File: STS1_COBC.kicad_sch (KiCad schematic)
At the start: 13 parts

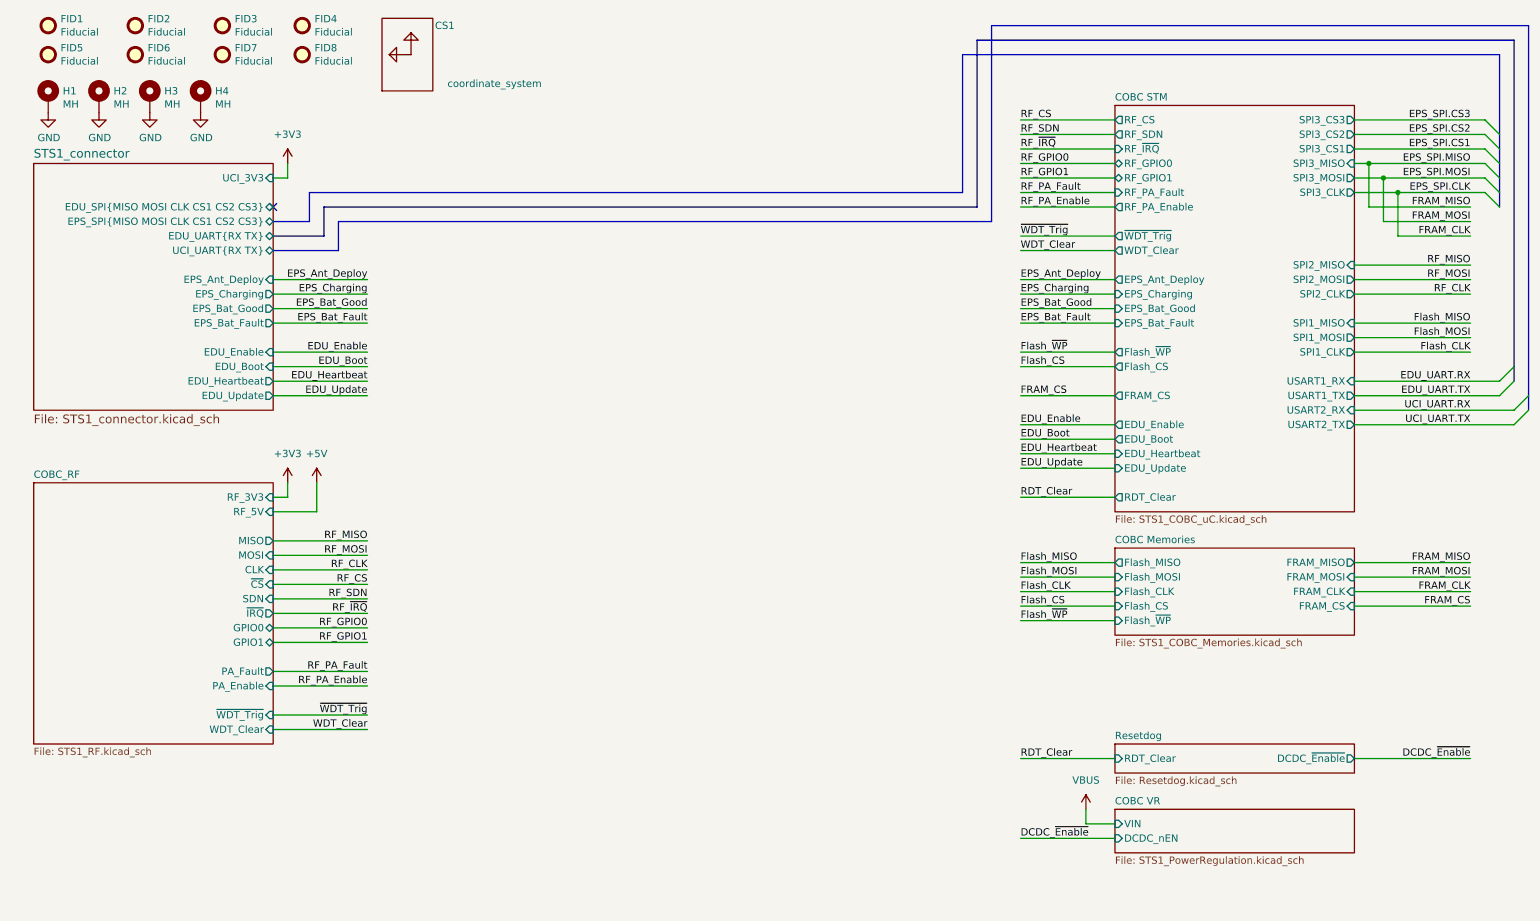
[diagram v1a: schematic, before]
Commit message: Reorganize and clean-up the components around the STM. Pinout changes: 1) Flash_CS moved from PB9 to PA4 2) Dosi_En added on PB10 3) EDU_Boot_Pin added on PB2 4) WDT_Clear moved from PA9 to PB9
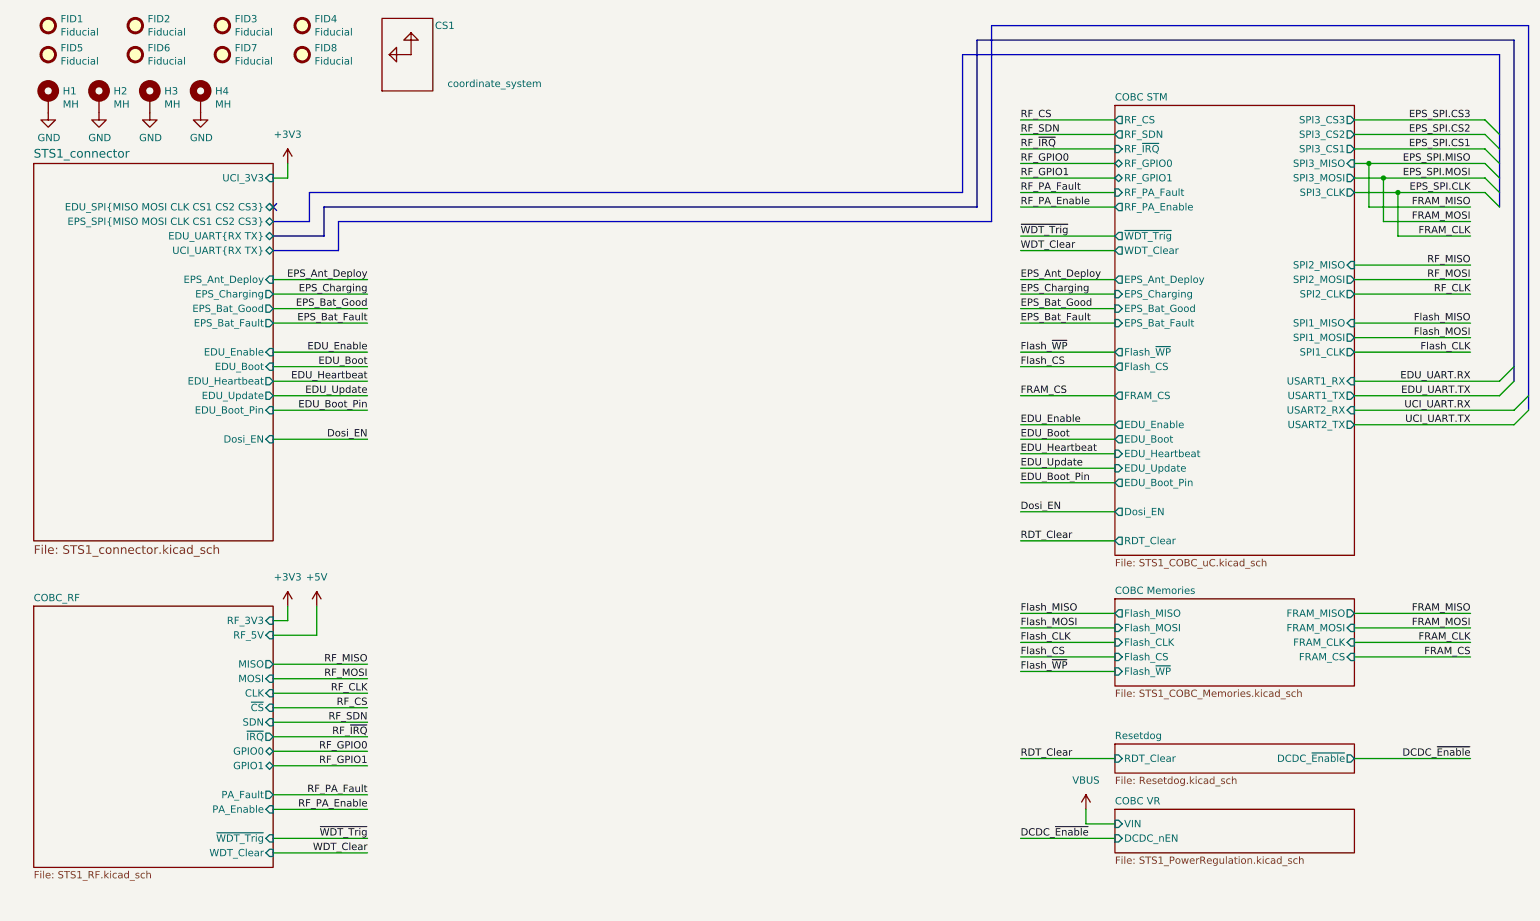
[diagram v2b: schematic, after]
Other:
- sheet COBC STM ports: added Dosi_EN, EDU_Boot_Pin; removed none
- sheet STS1_connector ports: added Dosi_EN, EDU_Boot_Pin; removed none

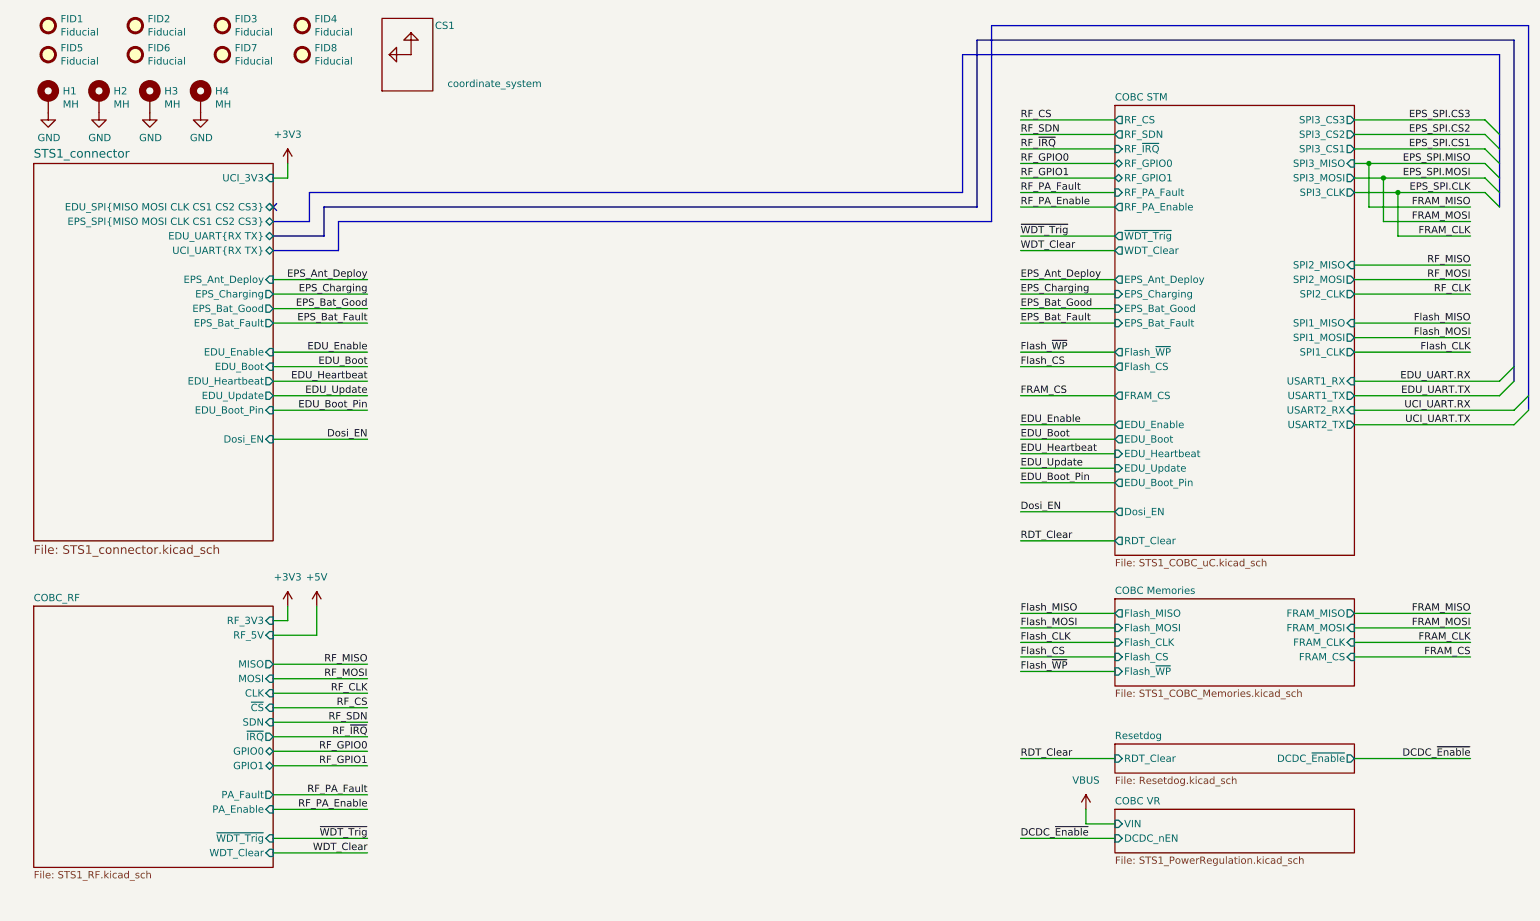
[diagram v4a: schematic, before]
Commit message: Add latchup protection circuits
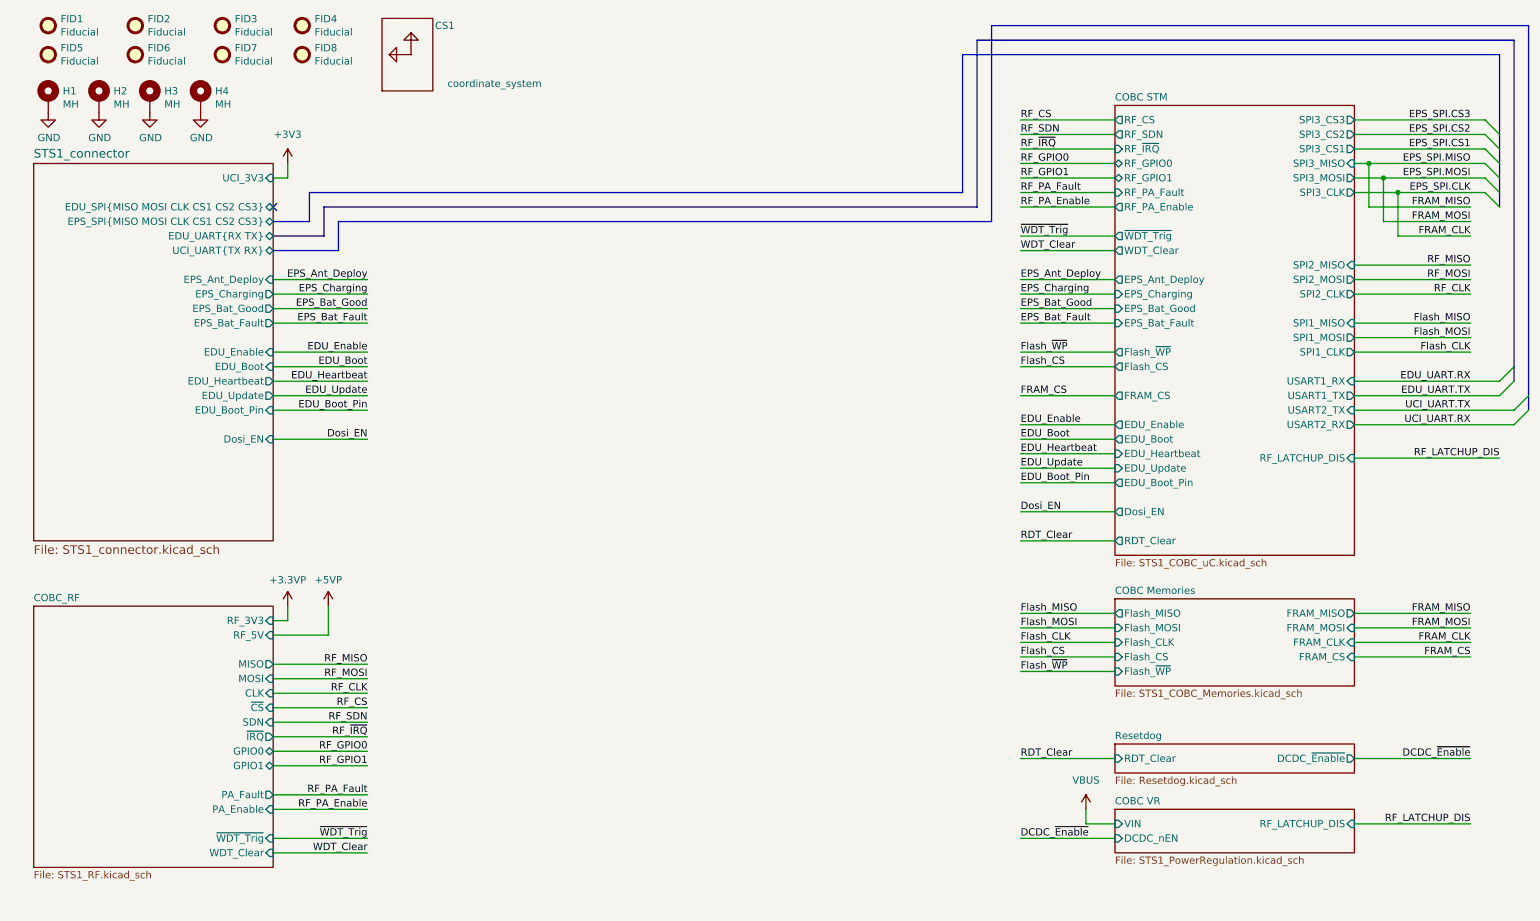
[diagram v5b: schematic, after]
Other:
- sheet COBC STM ports: added RF_LATCHUP_DIS; removed none
- sheet COBC VR ports: added RF_LATCHUP_DIS; removed none
- sheet STS1_connector ports: added UCI_UART{TX RX}; removed UCI_UART{RX TX}

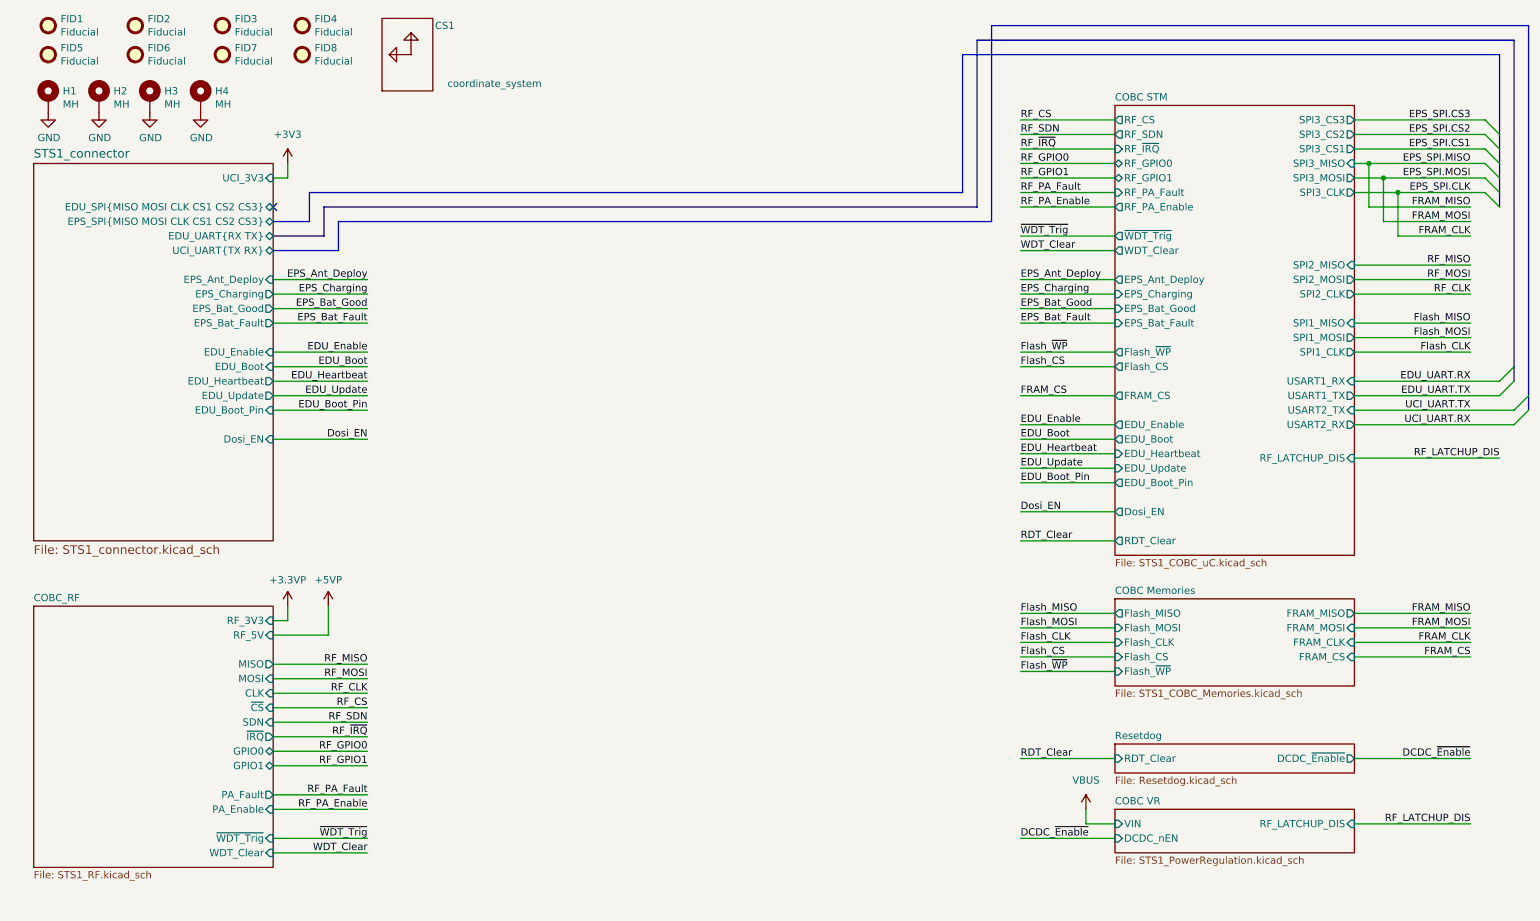
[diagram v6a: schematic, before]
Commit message: Add a temperature sensor near RF amplifier chip
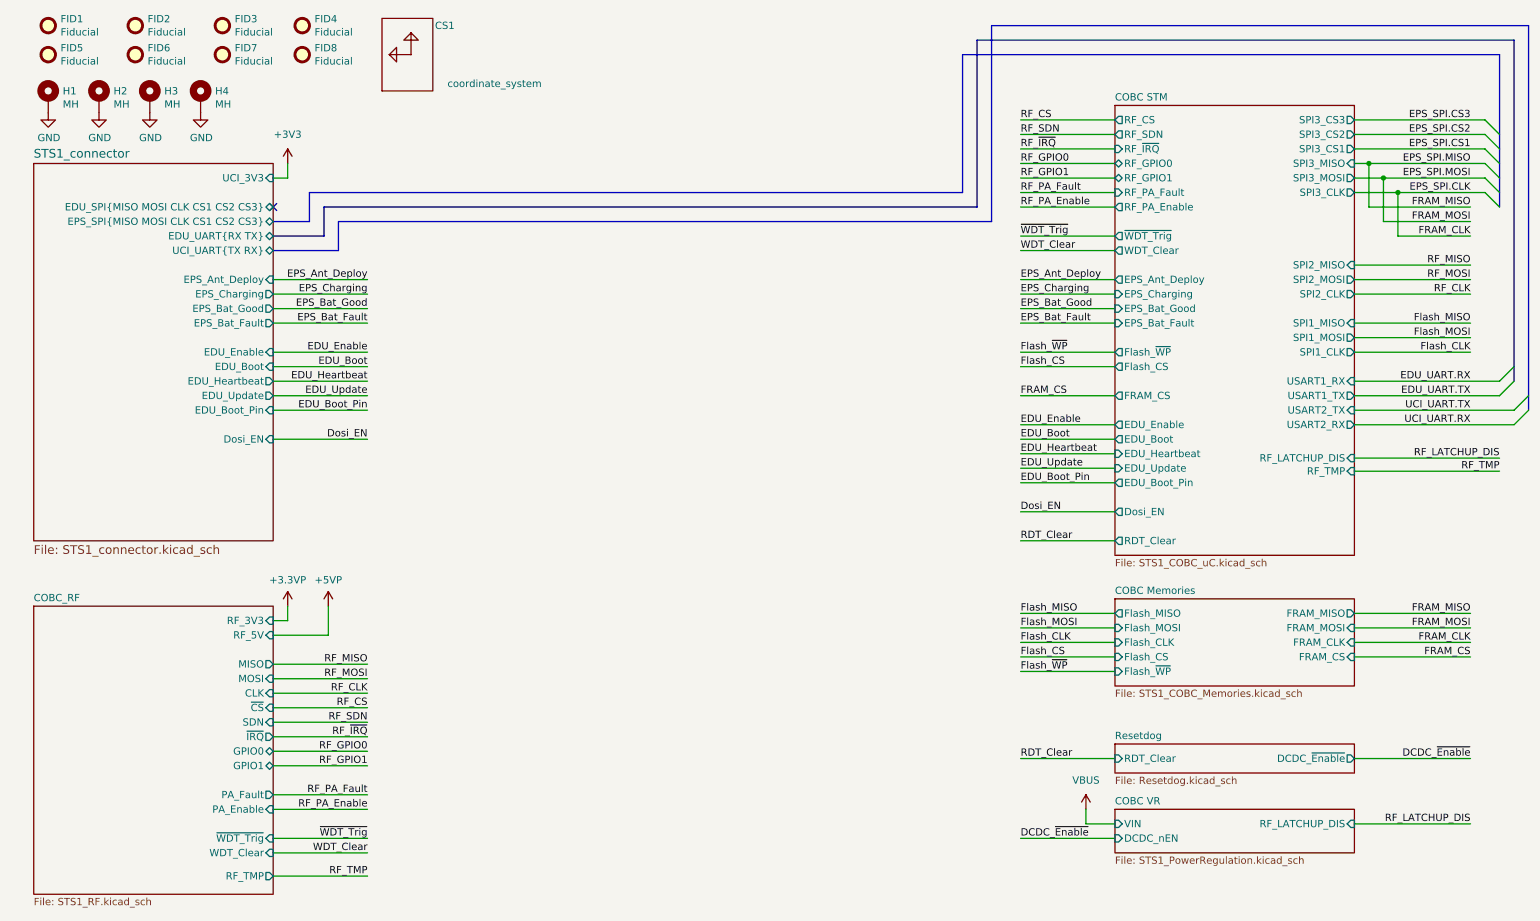
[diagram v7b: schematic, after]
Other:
- sheet COBC STM ports: added RF_TMP; removed none
- sheet COBC_RF ports: added RF_TMP; removed none
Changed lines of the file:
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@@
+    (stroke (width 0) (type default) (color 0 0 0 0))
+  )
+  (wire (pts (xy 246.38 93.218) (xy 271.78 93.218))
     (stroke (width 0) (type default) (color 0 0 0 0))
   )
@@
     (stroke (width 0) (type default) (color 0 0 0 0))
   )
+  (wire (pts (xy 57.15 164.084) (xy 73.66 164.084))
+    (stroke (width 0) (type default) (color 0 0 0 0))
+  )
   (wire (pts (xy 204.47 120.65) (xy 187.96 120.65))
     (stroke (width 0) (type default) (color 0 0 0 0))
@@
     (effects (font (size 1.27 1.27)) (justify right bottom))
   )
+  (label "RF_TMP" (at 271.78 93.218 180)
+    (effects (font (size 1.27 1.27)) (justify right bottom))
+  )
   (label "~{WDT_Trig}" (at 187.96 52.07 0)
     (effects (font (size 1.27 1.27)) (justify left bottom))
@@
   (label "DCDC_~{Enable}" (at 187.96 157.48 0)
     (effects (font (size 1.27 1.27)) (justify left bottom))
+  )
+  (label "RF_TMP" (at 73.66 164.084 180)
+    (effects (font (size 1.27 1.27)) (justify right bottom))
   )
   (label "EPS_SPI.CLK" (at 266.7 44.45 180)
@@
     )
   )
-  (sheet (at 15.24 116.84) (size 41.91 45.72) (fields_autoplaced)
+  (sheet (at 15.24 116.84) (size 41.91 50.419) (fields_autoplaced)
     (stroke (width 0.1524) (type solid) (color 0 0 0 0))
     (fill (color 0 0 0 0.0000))
@@
       (effects (font (size 1.27 1.27)) (justify left bottom))
     )
-    (property "Sheet file" "STS1_RF.kicad_sch" (id 1) (at 15.24 163.1446 0)
+    (property "Sheet file" "STS1_RF.kicad_sch" (id 1) (at 15.24 167.8436 0)
       (effects (font (size 1.27 1.27)) (justify left top))
     )
@@
     )
     (pin "WDT_Clear" input (at 57.15 160.02 0)
+      (effects (font (size 1.27 1.27)) (justify right))
+    )
+    (pin "RF_TMP" output (at 57.15 164.084 0)
       (effects (font (size 1.27 1.27)) (justify right))
     )
@@
     )
     (pin "RF_LATCHUP_DIS" input (at 246.38 90.932 0)
+      (effects (font (size 1.27 1.27)) (justify right))
+    )
+    (pin "RF_TMP" input (at 246.38 93.218 0)
       (effects (font (size 1.27 1.27)) (justify right))
     )
@@
       (reference "#PWR060") (unit 1) (value "GND") (footprint "")
     )
+    (path "/a8678e8a-595e-4c52-9d87-4220609965c5/cd099c17-a0a4-402b-a9aa-914e9e9f9e8d"
+      (reference "#PWR061") (unit 1) (value "GND") (footprint "")
+    )
+    (path "/a8678e8a-595e-4c52-9d87-4220609965c5/41d4b675-42ca-442a-aab2-5eabf608d38f"
+      (reference "#PWR062") (unit 1) (value "GND") (footprint "")
+    )
     (path "/be3cc363-80eb-4df5-9a1b-912085b5cf84/00000000-0000-0000-0000-00006130e947"
       (reference "#PWR066") (unit 1) (value "GND") (footprint "")
@@
       (reference "C93") (unit 1) (value "100n") (footprint "Capacitor_SMD:C_0603_1608Metric")
     )
+    (path "/a8678e8a-595e-4c52-9d87-4220609965c5/8fc4107a-a59b-4fbb-8f6b-a53c3a9995d7"
+      (reference "C94") (unit 1) (value "100n") (footprint "Capacitor_SMD:C_0603_1608Metric")
+    )
     (path "/00000000-0000-0000-0000-0000602f576d"
       (reference "CS1") (unit 1) (value "coordinate_system") (footprint "STS_connector:Coordinates")
@@
       (reference "U29") (unit 1) (value "NC7SZ32P5X-F22057") (footprint "STSLib:SOT65P210X110-5N")
     )
+    (path "/a8678e8a-595e-4c52-9d87-4220609965c5/767f449e-9616-4a18-a0a7-1d1ce5567d7b"
+      (reference "U30") (unit 1) (value "TMP36xS") (footprint "Package_TO_SOT_SMD:SOT-23-5")
+    )
     (path "/be3cc363-80eb-4df5-9a1b-912085b5cf84/00000000-0000-0000-0000-00006254c1e3"
